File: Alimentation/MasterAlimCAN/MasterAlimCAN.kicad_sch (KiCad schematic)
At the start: 51 parts, among them J1 I2C1_5, J10 Out U, J2 I2C2_5, J3 CAN1, J4 CAN2, J5 In App Prog, J6 DEBUG, J7 Conn AU, J8 Screw_Terminal_01x03, J9 Batt, SW1 RESET, SW2 BOOT0, U1 STM32G474RETx, U2 AMS1117-3.3, U3 MCP2558FD-xSN, Y1 16MHz

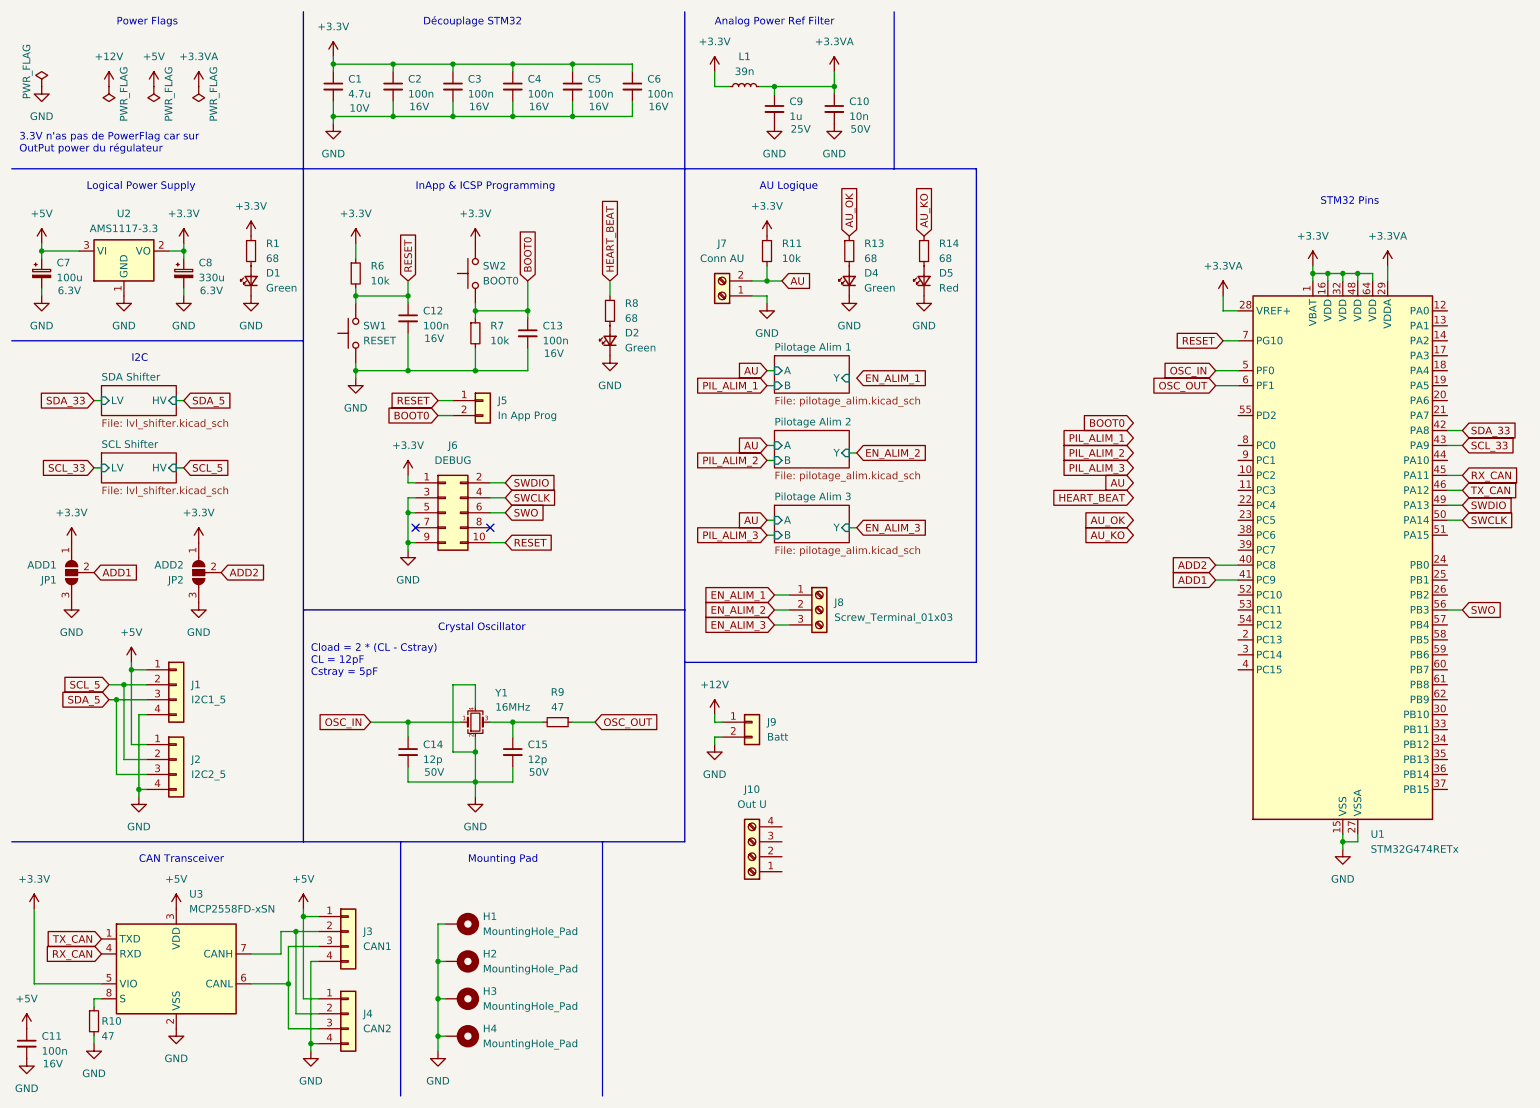
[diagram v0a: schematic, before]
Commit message: Restructure schematics of AlimCAN
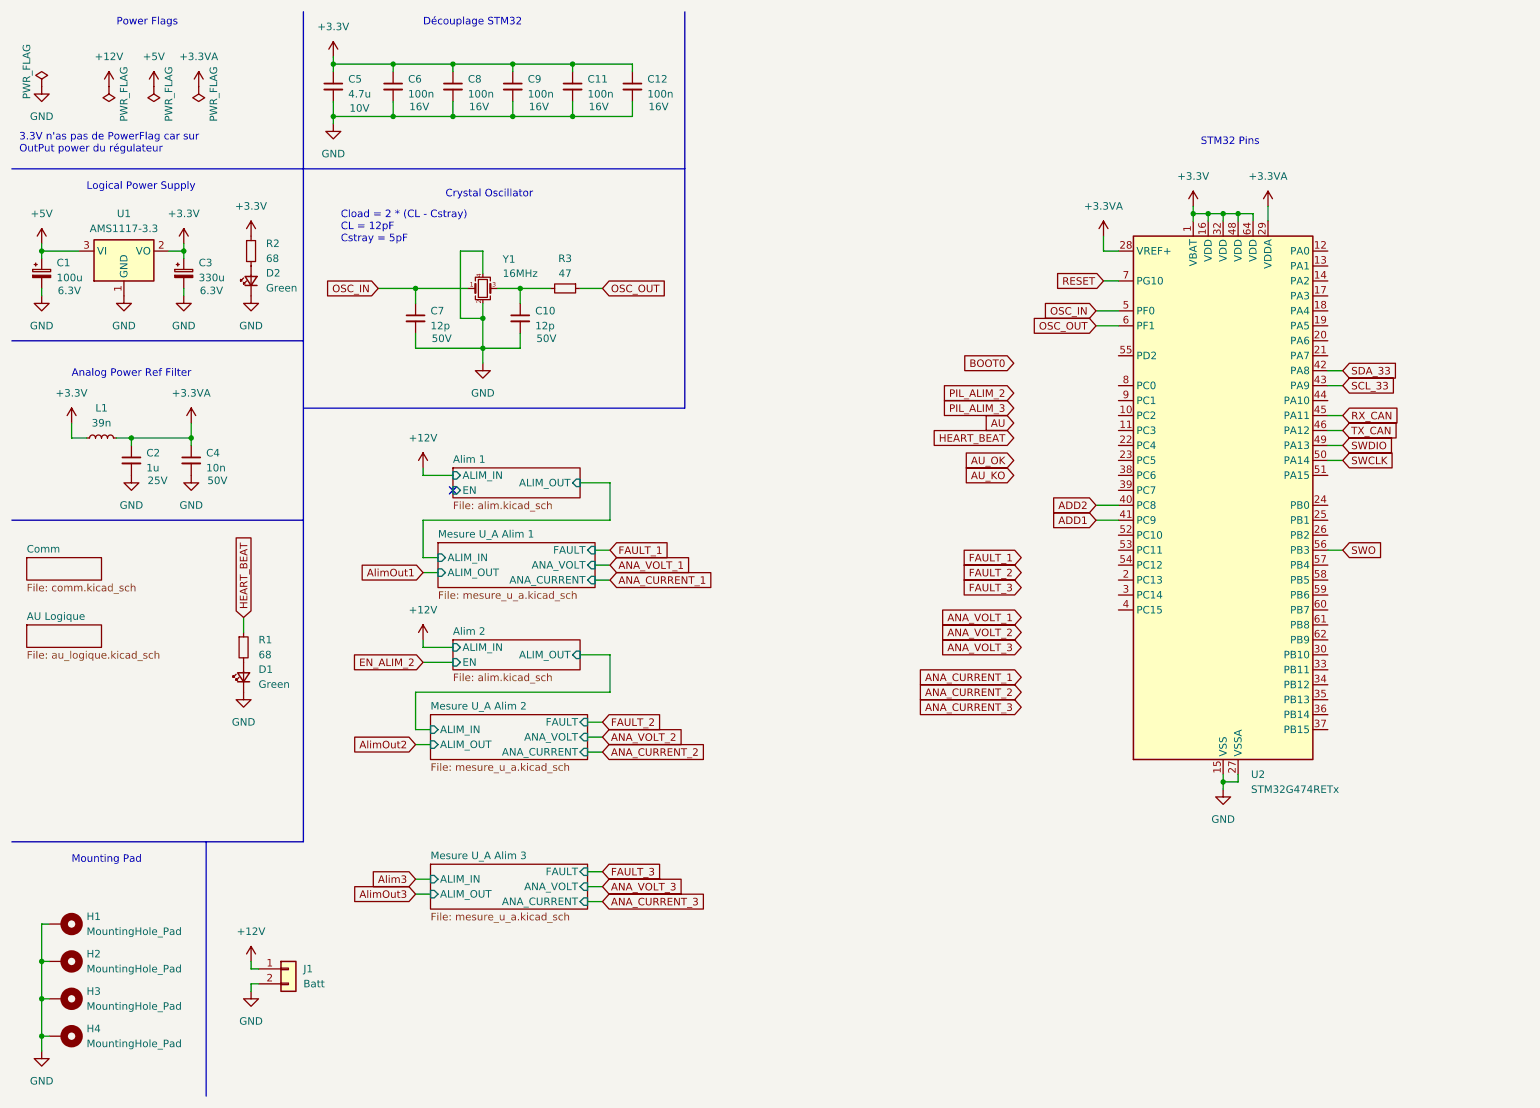
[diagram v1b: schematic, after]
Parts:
- removed C11, C12, C13: 100n, Capacitor_SMD:C_0402_1005Metric_Pad0.74x0.62mm_HandSolder, symbol Device:C_Small
- removed D4: Green, LED_SMD:LED_0805_2012Metric_Pad1.15x1.40mm_HandSolder, symbol Device:LED_Small
- removed D5: Red, LED_SMD:LED_0805_2012Metric_Pad1.15x1.40mm_HandSolder, symbol Device:LED_Small
- removed J1: I2C1_5, Connector_JST:JST_EH_S4B-EH_1x04_P2.50mm_Horizontal, symbol Connector_Generic:Conn_01x04
- removed J10: Out U, symbol Connector:Screw_Terminal_01x04
- removed J2: I2C2_5, Connector_JST:JST_EH_S4B-EH_1x04_P2.50mm_Horizontal, symbol Connector_Generic:Conn_01x04
- removed J3: CAN1, Connector_JST:JST_EH_S4B-EH_1x04_P2.50mm_Horizontal, symbol Connector_Generic:Conn_01x04
- removed J4: CAN2, Connector_JST:JST_EH_S4B-EH_1x04_P2.50mm_Horizontal, symbol Connector_Generic:Conn_01x04
- removed J5: In App Prog, Connector_JST:JST_EH_S2B-EH_1x02_P2.50mm_Horizontal, symbol Connector_Generic:Conn_01x02
- removed J6: DEBUG, Connector_PinHeader_1.27mm:PinHeader_2x05_P1.27mm_Vertical_SMD, symbol Connector_Generic:Conn_02x05_Odd_Even
- removed J7: Conn AU, TerminalBlock_Phoenix:TerminalBlock_Phoenix_MPT-0,5-2-2.54_1x02_P2.54mm_Horizontal, symbol Connector:Screw_Terminal_01x02
- removed J8: Screw_Terminal_01x03, symbol Connector:Screw_Terminal_01x03
- removed JP1: ADD1, Jumper:SolderJumper-3_P1.3mm_Open_RoundedPad1.0x1.5mm, symbol Jumper:SolderJumper_3_Open
- removed JP2: ADD2, Jumper:SolderJumper-3_P1.3mm_Open_RoundedPad1.0x1.5mm, symbol Jumper:SolderJumper_3_Open
- removed R10: 47, Resistor_SMD:R_0402_1005Metric_Pad0.72x0.64mm_HandSolder, symbol Device:R_Small
- removed R11, R6, R7: 10k, Resistor_SMD:R_0805_2012Metric_Pad1.20x1.40mm_HandSolder, symbol Device:R_Small
- removed R13, R14: 68, Resistor_SMD:R_0805_2012Metric_Pad1.20x1.40mm_HandSolder, symbol Device:R_Small
- removed SW1: RESET, ARIG:SW_TS_1088_AR_3x4x2, symbol Switch:SW_Push
- removed SW2: BOOT0, ARIG:SW_TS_1088_AR_3x4x2, symbol Switch:SW_Push
- removed U3: MCP2558FD-xSN, Package_SO:SOIC-8_3.9x4.9mm_P1.27mm, symbol Interface_CAN_LIN:MCP2558FD-xSN
- renumbered C7 to C1, C15 to C10, C5 to C11, C6 to C12, C9 to C2, C8 to C3, C10 to C4, C1 to C5, C2 to C6, C14 to C7, C3 to C8, C4 to C9, D2 to D1, D1 to D2, J9 to J1, R8 to R1, R1 to R2, R9 to R3, U2 to U1, U1 to U2
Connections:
- no-connect marks 2 -> 1
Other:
- removed sheet Pilotage Alim 1
- removed sheet Pilotage Alim 2
- removed sheet Pilotage Alim 3
- removed sheet SCL Shifter
- removed sheet SDA Shifter
- added sheet AU Logique (au_logique.kicad_sch)
- added sheet Alim 1 (alim.kicad_sch)
- added sheet Alim 2 (alim.kicad_sch)
- added sheet Comm (comm.kicad_sch)
- added sheet Mesure U_A Alim 1 (mesure_u_a.kicad_sch)
- added sheet Mesure U_A Alim 2 (mesure_u_a.kicad_sch)
- added sheet Mesure U_A Alim 3 (mesure_u_a.kicad_sch)
- note removed: "AU Logique"
- note removed: "CAN Transceiver"
- note removed: "I2C"
- note removed: "InApp & ICSP Programming"
- moved on the sheet: C10, C2, C4, C7, D1, H1, H2, H3, H4, J1, L1, R1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

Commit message: Init placement for MasterAlimCAN
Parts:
- removed J1: Batt, Connector_AMASS:AMASS_XT60-F_1x02_P7.20mm_Vertical, symbol Connector_Generic:Conn_01x02
- added J1: BATT, TerminalBlock_Phoenix:TerminalBlock_Phoenix_MKDS-1,5-2-5.08_1x02_P5.08mm_Horizontal, symbol Connector:Screw_Terminal_01x02
- added J10: Alim OUT, TerminalBlock_Phoenix:TerminalBlock_Phoenix_MKDS-1,5-4-5.08_1x04_P5.08mm_Horizontal, symbol Connector:Screw_Terminal_01x04
- added J11: ALIM 3 IN, TerminalBlock_Phoenix:TerminalBlock_Phoenix_MKDS-1,5-2-5.08_1x02_P5.08mm_Horizontal, symbol Connector:Screw_Terminal_01x02
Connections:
- net +12V: now also J1.1 (Pin_1)
- net +5V: now also J10.1 (Pin_1)
- net ANA_CURRENT_1: now also U2.13 (PA1)
- net ANA_CURRENT_2: now also U2.17 (PA3)
- net ANA_CURRENT_3: now also U2.21 (PA7)
- net ANA_VOLT_1: now also U2.12 (PA0)
- net ANA_VOLT_2: now also U2.14 (PA2)
- net ANA_VOLT_3: now also U2.20 (PA6)
- net AU: now also U2.37 (PB15)
- net AU_KO: now also U2.33 (PB11)
- net AU_OK: now also U2.35 (PB13)
- net Alim3: now also J11.1 (Pin_1)
- net AlimOut2: now also J10.2 (Pin_2)
- net AlimOut3: now also J10.4 (Pin_4)
- net BOOT0: now also U2.61 (PB8)
- net FAULT_1: now also U2.11 (PC3)
- net FAULT_2: now also U2.18 (PA4)
- net FAULT_3: now also U2.19 (PA5)
- net GND: now also J1.2 (Pin_2), J10.3 (Pin_3), J11.2 (Pin_2)
- net HEART_BEAT: now also U2.39 (PC7)
- net PIL_ALIM_2: now also U2.24 (PB0)
- net PIL_ALIM_3: now also U2.25 (PB1)
- no-connect marks 1 -> 25

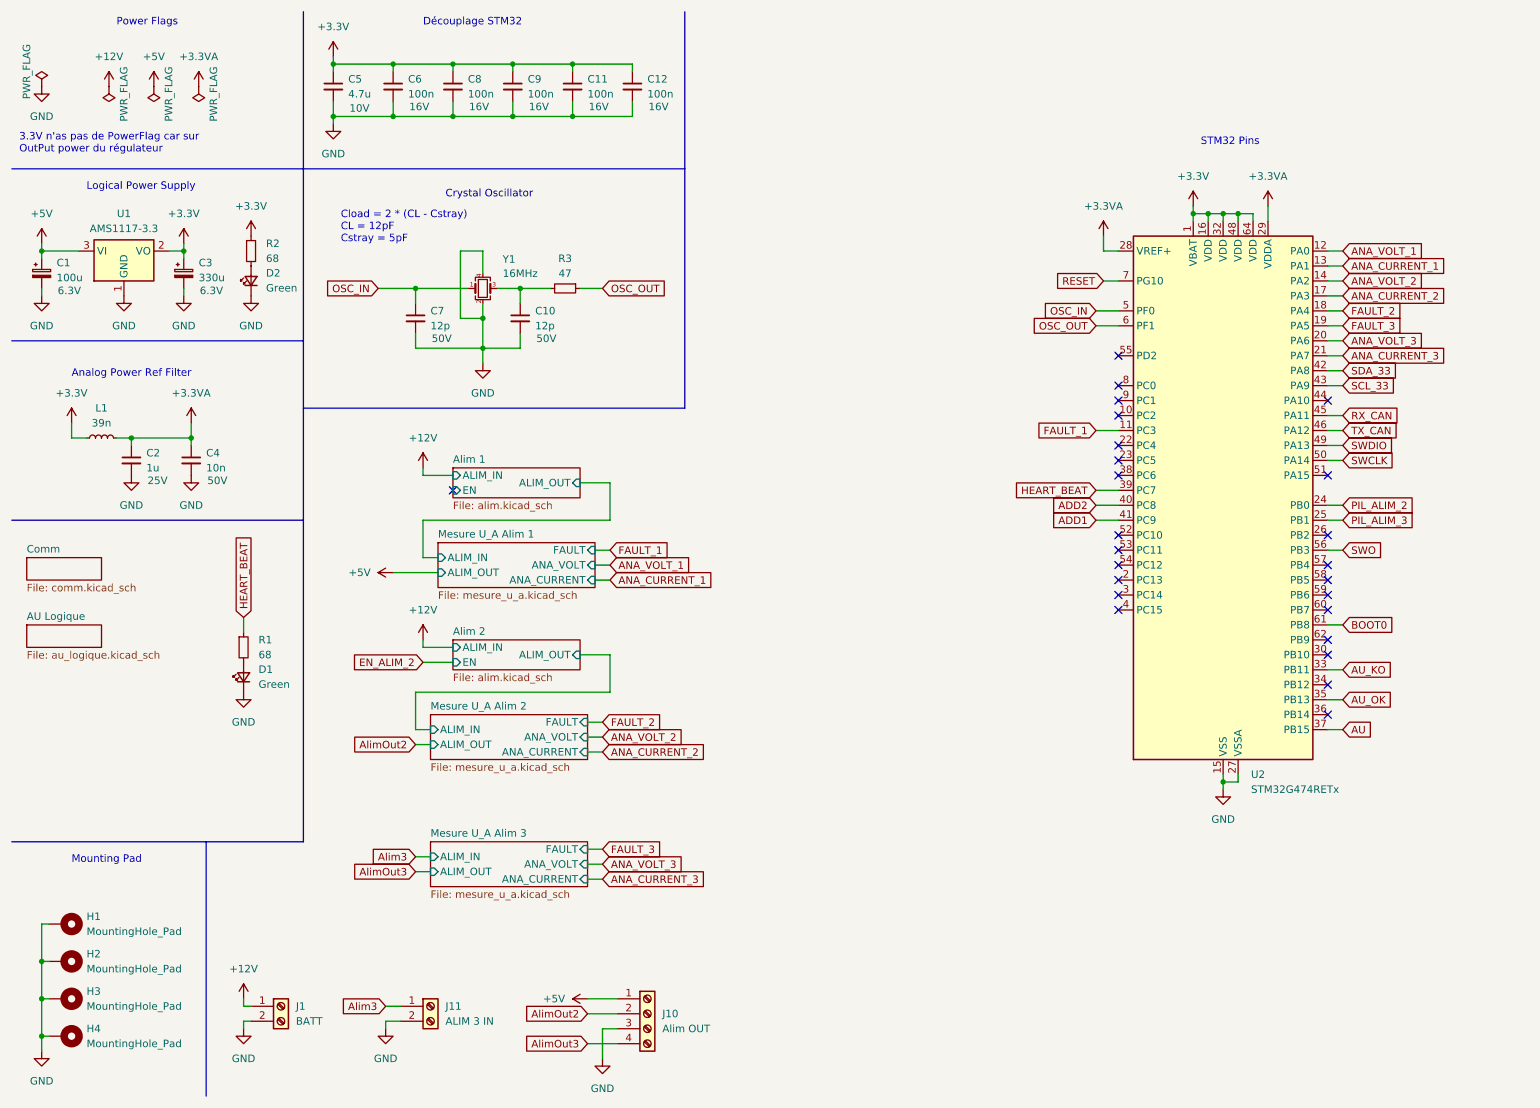
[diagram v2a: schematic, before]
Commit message: New disposition for alim CAN
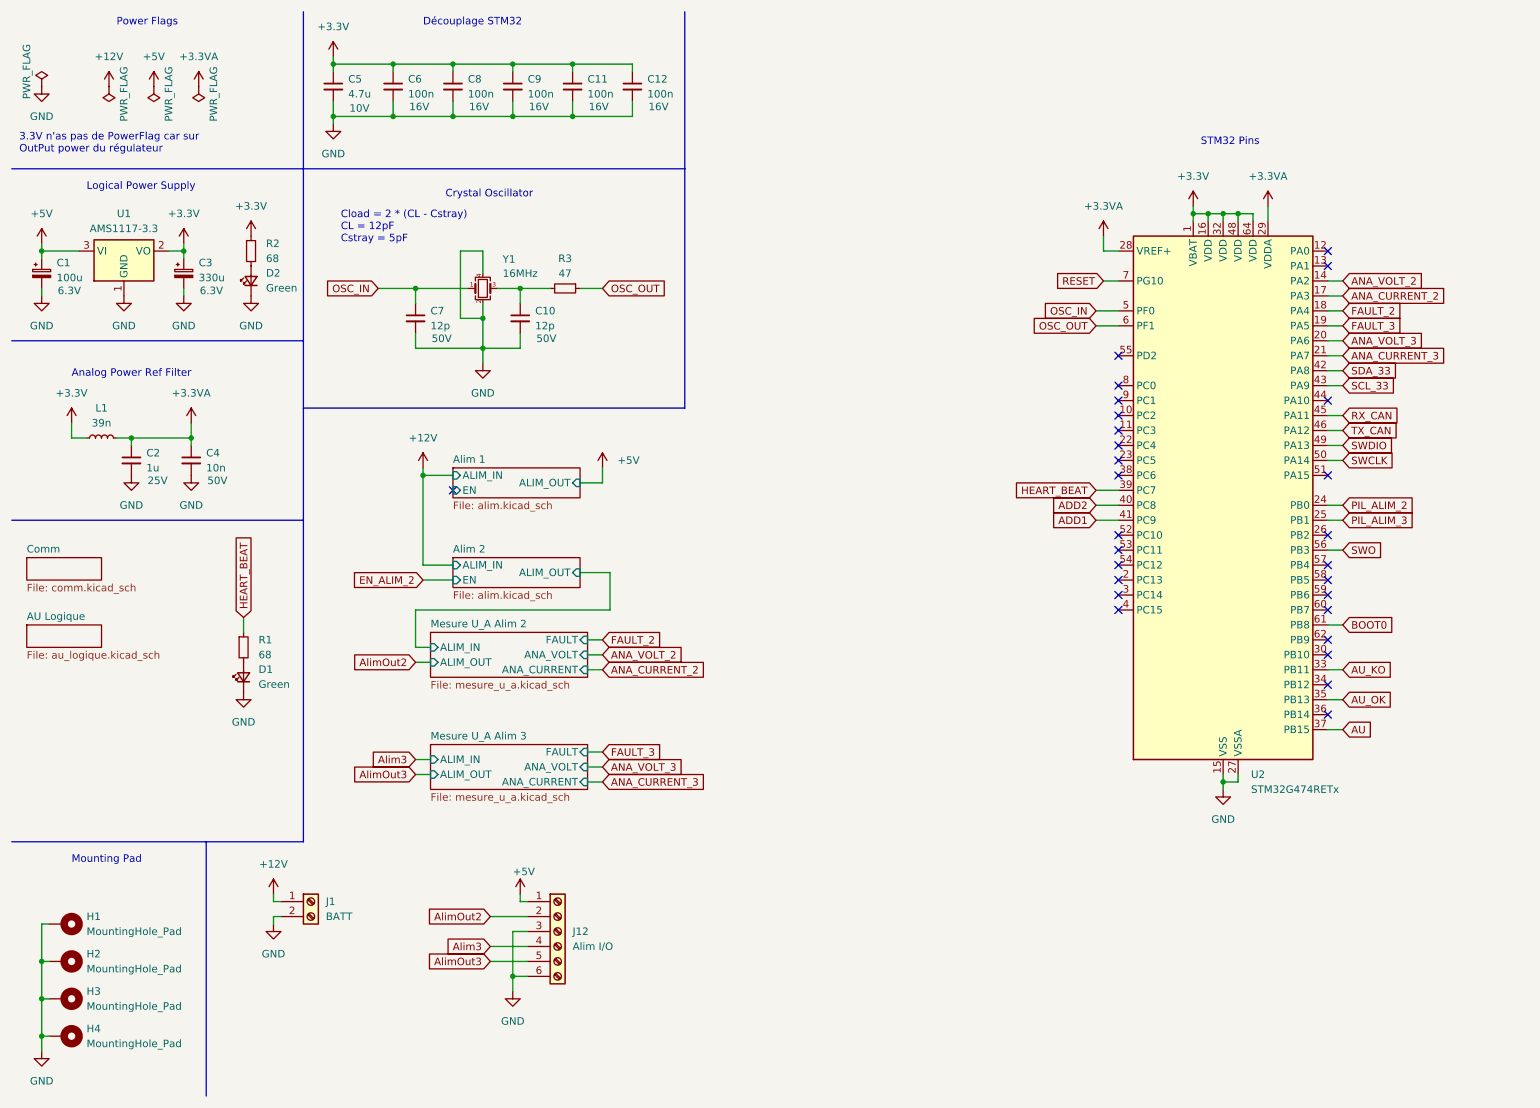
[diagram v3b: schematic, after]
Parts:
- removed J10: Alim OUT, TerminalBlock_Phoenix:TerminalBlock_Phoenix_MKDS-1,5-4-5.08_1x04_P5.08mm_Horizontal, symbol Connector:Screw_Terminal_01x04
- removed J11: ALIM 3 IN, TerminalBlock_Phoenix:TerminalBlock_Phoenix_MKDS-1,5-2-5.08_1x02_P5.08mm_Horizontal, symbol Connector:Screw_Terminal_01x02
- added J12: Alim I/O, TerminalBlock_Phoenix:TerminalBlock_Phoenix_MKDS-1,5-6-5.08_1x06_P5.08mm_Horizontal, symbol Connector:Screw_Terminal_01x06
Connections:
- net +5V: now also J12.1 (Pin_1)
- net Alim3: now also J12.4 (Pin_4)
- net AlimOut2: now also J12.2 (Pin_2)
- net AlimOut3: now also J12.5 (Pin_5)
- net GND: now also J12.3 (Pin_3), J12.6 (Pin_6)
- net ANA_CURRENT_1: no longer names the net of U2.13 (PA1)
- net ANA_VOLT_1: no longer names the net of U2.12 (PA0)
- net FAULT_1: no longer names the net of U2.11 (PC3)
- no-connect marks 25 -> 28
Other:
- removed sheet Mesure U_A Alim 1
- moved on the sheet: J1
